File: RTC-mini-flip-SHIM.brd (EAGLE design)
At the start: 17.8 x 20.3 mm, 9 parts, among them IC1 DS3231/SO

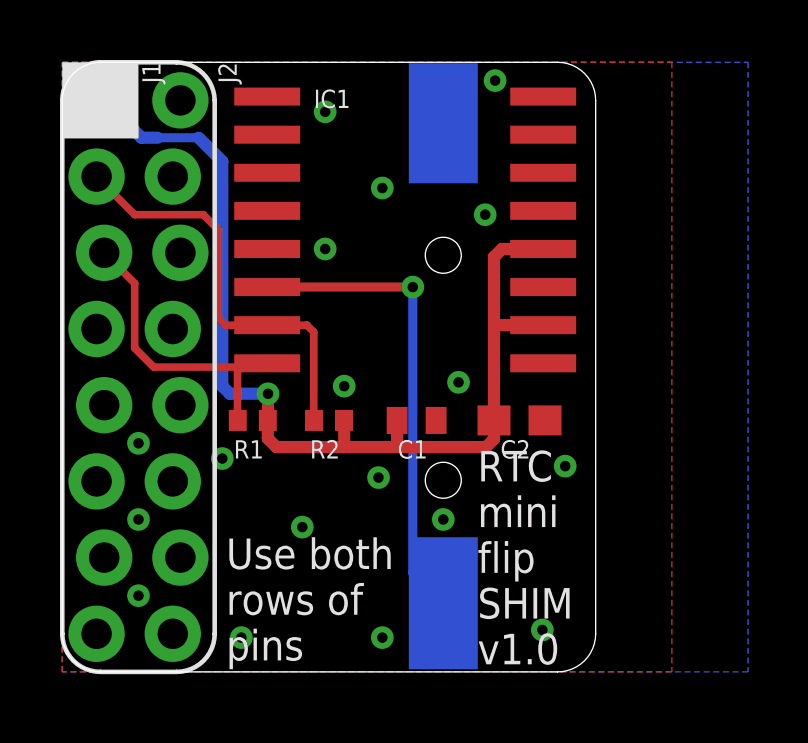
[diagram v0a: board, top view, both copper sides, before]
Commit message: Removed unneeded traces. generated new CAM.
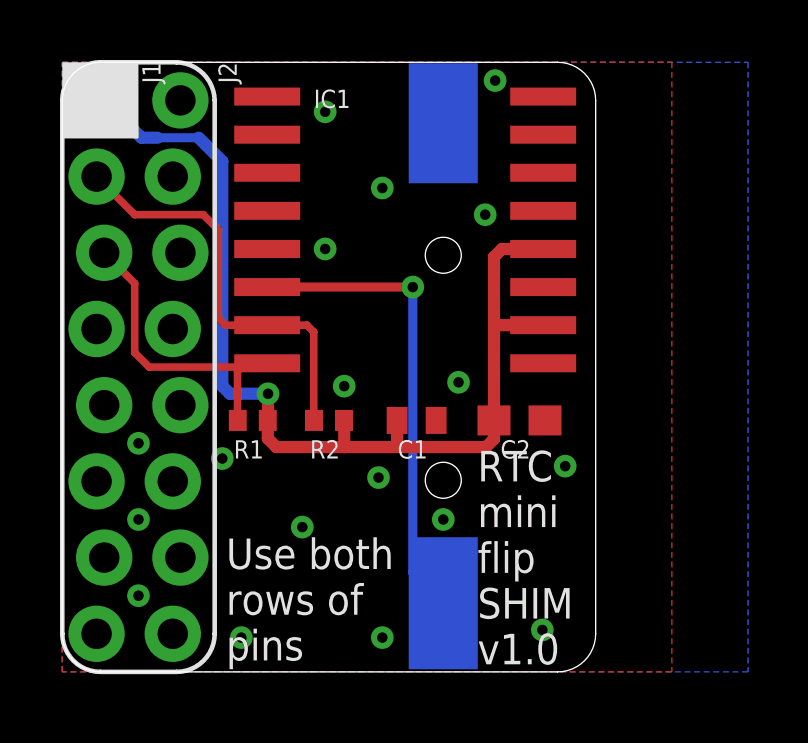
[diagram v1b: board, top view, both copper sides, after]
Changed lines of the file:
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@@
 <drawing>
 <settings>
-<setting alwaysvectorfont="yes"/>
+<setting alwaysvectorfont="no"/>
 <setting verticaltext="up"/>
 </settings>
@@
 <wire x1="6.096" y1="10.287" x2="6.83" y2="10.287" width="0.254" layer="1"/>
 <wire x1="1.397" y1="13.97" x2="2.413" y2="12.954" width="0.254" layer="1"/>
-<wire x1="2.413" y1="12.954" x2="2.413" y2="10.795" width="0.254" layer="1"/>
-<wire x1="2.413" y1="10.795" x2="3.048" y2="10.16" width="0.254" layer="1"/>
+<wire x1="2.413" y1="12.954" x2="2.413" y2="10.6426" width="0.254" layer="1"/>
+<wire x1="2.413" y1="10.6426" x2="2.8956" y2="10.16" width="0.254" layer="1"/>
 <wire x1="6.703" y1="10.16" x2="6.83" y2="10.287" width="0.254" layer="1"/>
-<wire x1="3.048" y1="10.16" x2="6.703" y2="10.16" width="0.254" layer="1"/>
+<wire x1="2.8956" y1="10.16" x2="6.703" y2="10.16" width="0.254" layer="1"/>
 </signal>
 <signal name="SDA">

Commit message: Added battery connector. Generated CAM.
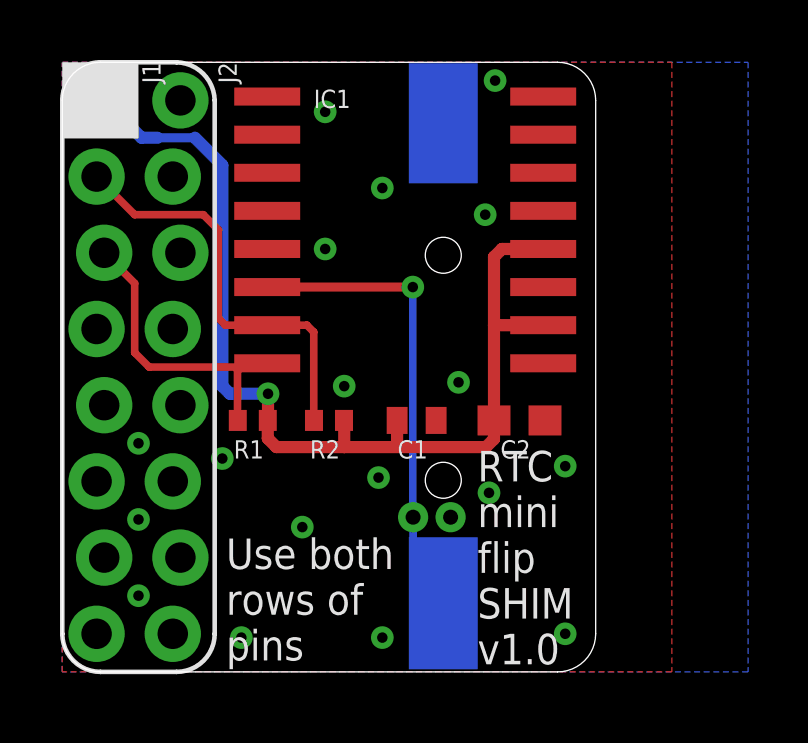
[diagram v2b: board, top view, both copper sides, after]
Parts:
- added LIPO1: Molex VERT 1.25mm pitch, PiB_connectors:_MOLEX-0530470210_VERT_PITCH-1.25MM
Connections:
- net GND: now also LIPO1.2
- net VBAT: now also LIPO1.1
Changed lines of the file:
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@@
 <drawing>
 <settings>
-<setting alwaysvectorfont="no"/>
+<setting alwaysvectorfont="yes"/>
 <setting verticaltext="up"/>
 </settings>
@@
 <layer number="154" name="FabDoc2" color="2" fill="1" visible="no" active="no"/>
 <layer number="155" name="FabDoc3" color="7" fill="15" visible="no" active="no"/>
+<layer number="160" name="tMountFaceplate" color="7" fill="1" visible="yes" active="yes"/>
+<layer number="161" name="bMountFaceplate" color="7" fill="1" visible="yes" active="yes"/>
+<layer number="162" name="tCopperArt" color="7" fill="1" visible="yes" active="yes"/>
+<layer number="163" name="bCopperArt" color="7" fill="1" visible="yes" active="yes"/>
+<layer number="164" name="tRubout" color="7" fill="1" visible="yes" active="yes"/>
+<layer number="165" name="bRubout" color="7" fill="1" visible="yes" active="yes"/>
+<layer number="167" name="Fiducials" color="7" fill="1" visible="yes" active="yes"/>
+<layer number="169" name="internal" color="7" fill="1" visible="yes" active="yes"/>
 <layer number="199" name="Contour" color="7" fill="1" visible="no" active="yes"/>
 <layer number="200" name="200bmp" color="1" fill="10" visible="no" active="yes"/>
@@
 </element>
 <element name="LOGO1" library="_my_logos" package="MFDEC_L_10MM" value="MFDECLOGO_L_10MM" x="21.336" y="3.683" smashed="yes" rot="MR0"/>
+<element name="LIPO1" library="PiB_connectors" package="_MOLEX-0530470210_VERT_PITCH-1.25MM" package3d_urn="urn:adsk.eagle:package:2973718/3" value="Molex VERT 1.25mm pitch" x="12.319" y="5.1562" smashed="yes" rot="MR180">
+<attribute name="DATASHEET_CONNECTOR1" value="https://www.molex.com/pdm_docs/sd/530470210_sd.pdf" x="12.319" y="5.1562" size="1.778" layer="28" rot="MR180" display="off"/>
+<attribute name="DATASHEET_CONNECTOR2" value="https://www.molex.com/pdm_docs/sd/510210700_sd.pdf" x="12.319" y="5.1562" size="1.778" layer="28" rot="MR180" display="off"/>
+<attribute name="DATASHEET_CRIMP" value="https://www.molex.com/pdm_docs/sd/500798000_sd.pdf" x="12.319" y="5.1562" size="1.778" layer="28" rot="MR180" display="off"/>
+<attribute name="DISTLINK_CONNECTOR1" value="https://www.digikey.com/products/en?keywords=WM1731-ND" x="12.319" y="5.1562" size="1.778" layer="28" rot="MR180" display="off"/>
+<attribute name="DISTLINK_CONNECTOR2" value="https://www.digikey.com/products/en?keywords=WM1720-ND" x="12.319" y="5.1562" size="1.778" layer="28" rot="MR180" display="off"/>
+<attribute name="DISTLINK_CRIMP" value="https://www.digikey.com/products/en?keywords=WM1142CT-ND" x="12.319" y="5.1562" size="1.778" layer="28" rot="MR180" display="off"/>
+<attribute name="DISTPN_CONNECTOR1" value="WM1731-ND" x="12.319" y="5.1562" size="1.778" layer="28" rot="MR180" display="off"/>
+<attribute name="DISTPN_CONNECTOR2" value="WM1720-ND" x="12.319" y="5.1562" size="1.778" layer="28" rot="MR180" display="off"/>
+<attribute name="DISTPN_CRIMP" value="WM1142CT-ND" x="12.319" y="5.1562" size="1.778" layer="28" rot="MR180" display="off"/>
+<attribute name="DIST_CONNECTOR1" value="Digikey" x="12.319" y="5.1562" size="1.778" layer="28" rot="MR180" display="off"/>
+<attribute name="DIST_CONNECTOR2" value="Digikey" x="12.319" y="5.1562" size="1.778" layer="28" rot="MR180" display="off"/>
+<attribute name="DIST_CRIMP" value="Digikey" x="12.319" y="5.1562" size="1.778" layer="28" rot="MR180" display="off"/>
+<attribute name="MFR_CONNECTOR1" value="Molex, LLC" x="12.319" y="5.1562" size="1.778" layer="28" rot="MR180" display="off"/>
+<attribute name="MFR_CONNECTOR2" value="Molex, LLC" x="12.319" y="5.1562" size="1.778" layer="28" rot="MR180" display="off"/>
+<attribute name="MFR_CRIMP" value="Molex, LLC" x="12.319" y="5.1562" size="1.778" layer="28" rot="MR180" display="off"/>
+<attribute name="MPN_CONNECTOR1" value="0530470210" x="12.319" y="5.1562" size="1.778" layer="28" rot="MR180" display="off"/>
+<attribute name="MPN_CONNECTOR2" value="51021-0200" x="12.319" y="5.1562" size="1.778" layer="28" rot="MR180" display="off"/>
+<attribute name="MPN_CRIMP" value="0500798000" x="12.319" y="5.1562" size="1.778" layer="28" rot="MR180" display="off"/>
+<attribute name="NAME" x="12.319" y="6.4262" size="0.5" layer="26" font="vector" ratio="10" rot="MR180" align="top-center"/>
+<attribute name="VALUE" x="12.319" y="4.3942" size="0.25" layer="28" font="vector" ratio="10" rot="MR180" align="bottom-center"/>
+</element>
 </elements>
 <signals>
@@
 <wire x1="6.83" y1="12.827" x2="11.684" y2="12.827" width="0.3048" layer="1"/>
 <via x="11.684" y="12.827" extent="1-16" drill="0.35"/>
-<wire x1="11.684" y1="12.827" x2="11.684" y2="3.303" width="0.3048" layer="16"/>
-<wire x1="11.684" y1="3.303" x2="12.7" y2="2.287" width="0.3048" layer="16"/>
+<contactref element="LIPO1" pad="1"/>
+<wire x1="11.684" y1="12.827" x2="11.684" y2="5.1662" width="0.254" layer="16"/>
+<wire x1="11.684" y1="5.1662" x2="11.694" y2="5.1562" width="0.254" layer="16"/>
+<wire x1="11.694" y1="5.1562" x2="11.694" y2="3.293" width="0.254" layer="16"/>
+<wire x1="11.694" y1="3.293" x2="12.7" y2="2.287" width="0.254" layer="16"/>
 </signal>
 <signal name="SCL">
@@
 <wire x1="1.397" y1="19.05" x2="2.6416" y2="17.8054" width="0.4064" layer="16"/>
 <wire x1="2.6416" y1="17.8054" x2="3.175" y2="17.8054" width="0.4064" layer="16"/>
-<wire x1="3.175" y1="17.8054" x2="4.5466" y2="17.8054" width="0.3048" layer="16"/>
-<wire x1="4.5466" y1="17.8054" x2="4.572" y2="17.78" width="0.3048" layer="16"/>
-<wire x1="4.5466" y1="17.8054" x2="5.334" y2="17.018" width="0.4064" layer="16"/>
-<wire x1="5.334" y1="17.018" x2="5.334" y2="9.525" width="0.4064" layer="16"/>
+<wire x1="3.175" y1="17.8054" x2="4.4196" y2="17.8054" width="0.3048" layer="16"/>
+<wire x1="4.4196" y1="17.8054" x2="5.334" y2="16.891" width="0.4064" layer="16"/>
+<wire x1="5.334" y1="16.891" x2="5.334" y2="9.525" width="0.4064" layer="16"/>
 <wire x1="5.334" y1="9.525" x2="5.588" y2="9.271" width="0.4064" layer="16"/>
 <wire x1="5.588" y1="9.271" x2="6.858" y2="9.271" width="0.4064" layer="16"/>
@@
 <via x="9.398" y="9.525" extent="1-16" drill="0.35"/>
 <via x="16.764" y="6.858" extent="1-16" drill="0.35"/>
-<via x="16.002" y="1.397" extent="1-16" drill="0.35"/>
+<via x="16.764" y="1.27" extent="1-16" drill="0.35"/>
 <via x="10.668" y="1.143" extent="1-16" drill="0.35"/>
 <via x="5.969" y="1.143" extent="1-16" drill="0.35"/>
-<via x="12.7" y="5.08" extent="1-16" drill="0.35"/>
+<via x="14.224" y="5.969" extent="1-16" drill="0.35"/>
 <via x="10.541" y="6.477" extent="1-16" drill="0.35"/>
 <via x="5.334" y="7.112" extent="1-16" drill="0.35"/>
 <via x="8.001" y="4.826" extent="1-16" drill="0.35"/>
 <via x="14.4272" y="19.7104" extent="1-16" drill="0.35"/>
+<contactref element="LIPO1" pad="2"/>
 </signal>
 </signals>
